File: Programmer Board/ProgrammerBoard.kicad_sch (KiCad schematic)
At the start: 9 parts

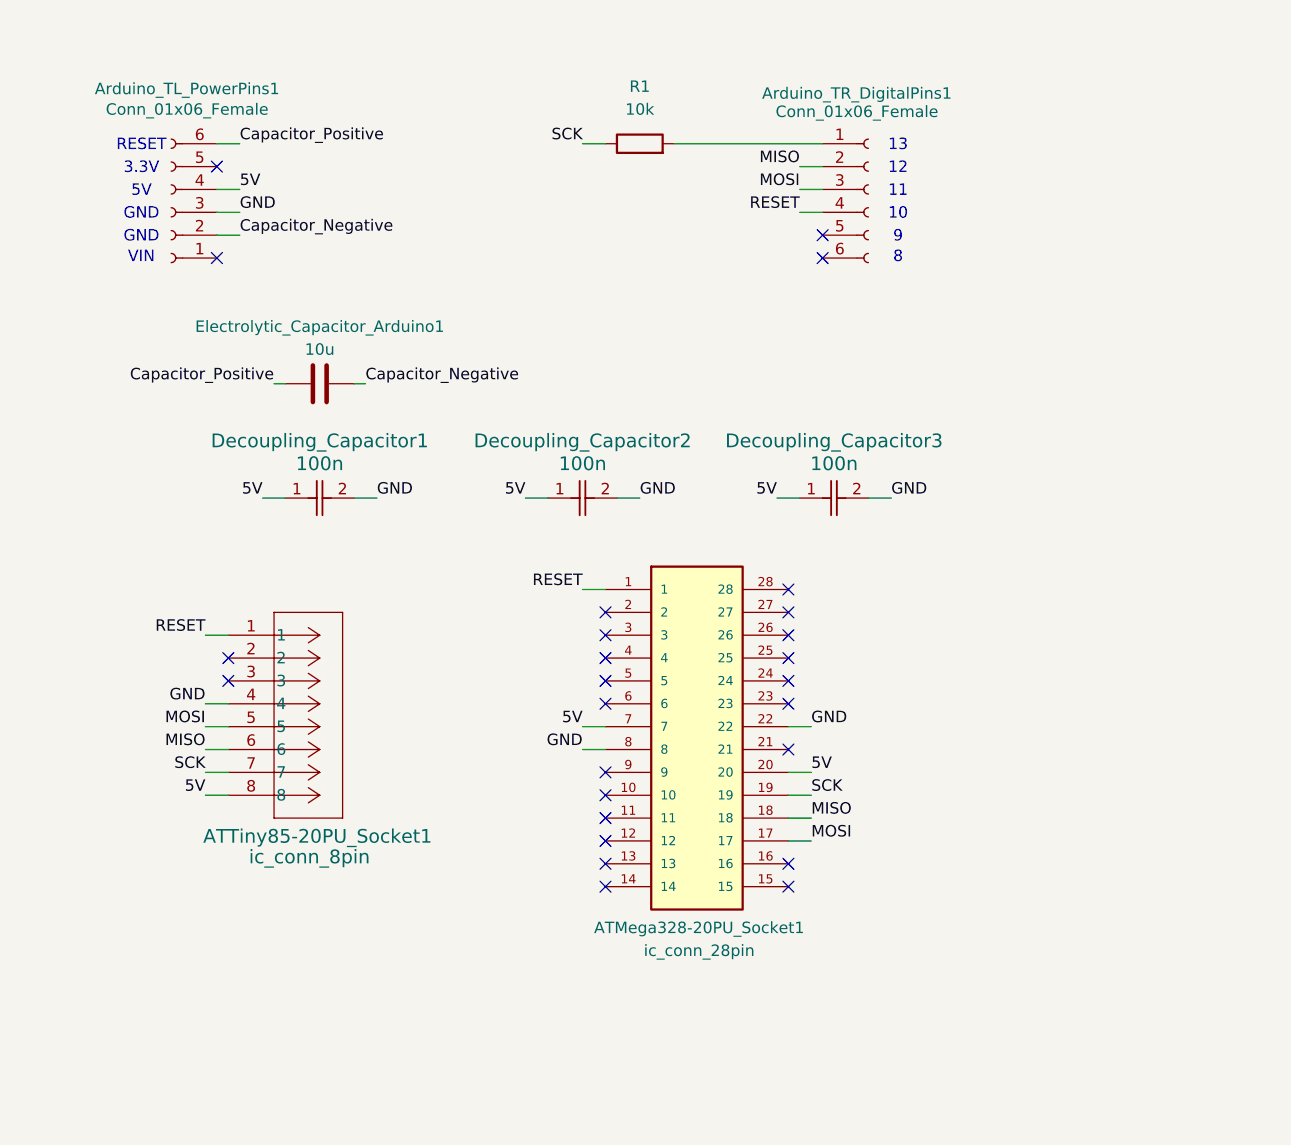
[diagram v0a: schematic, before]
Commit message: Added Header Socket Pins 1x4, 1x6, 1x8
- For flush attachment to Arduino Uno R3
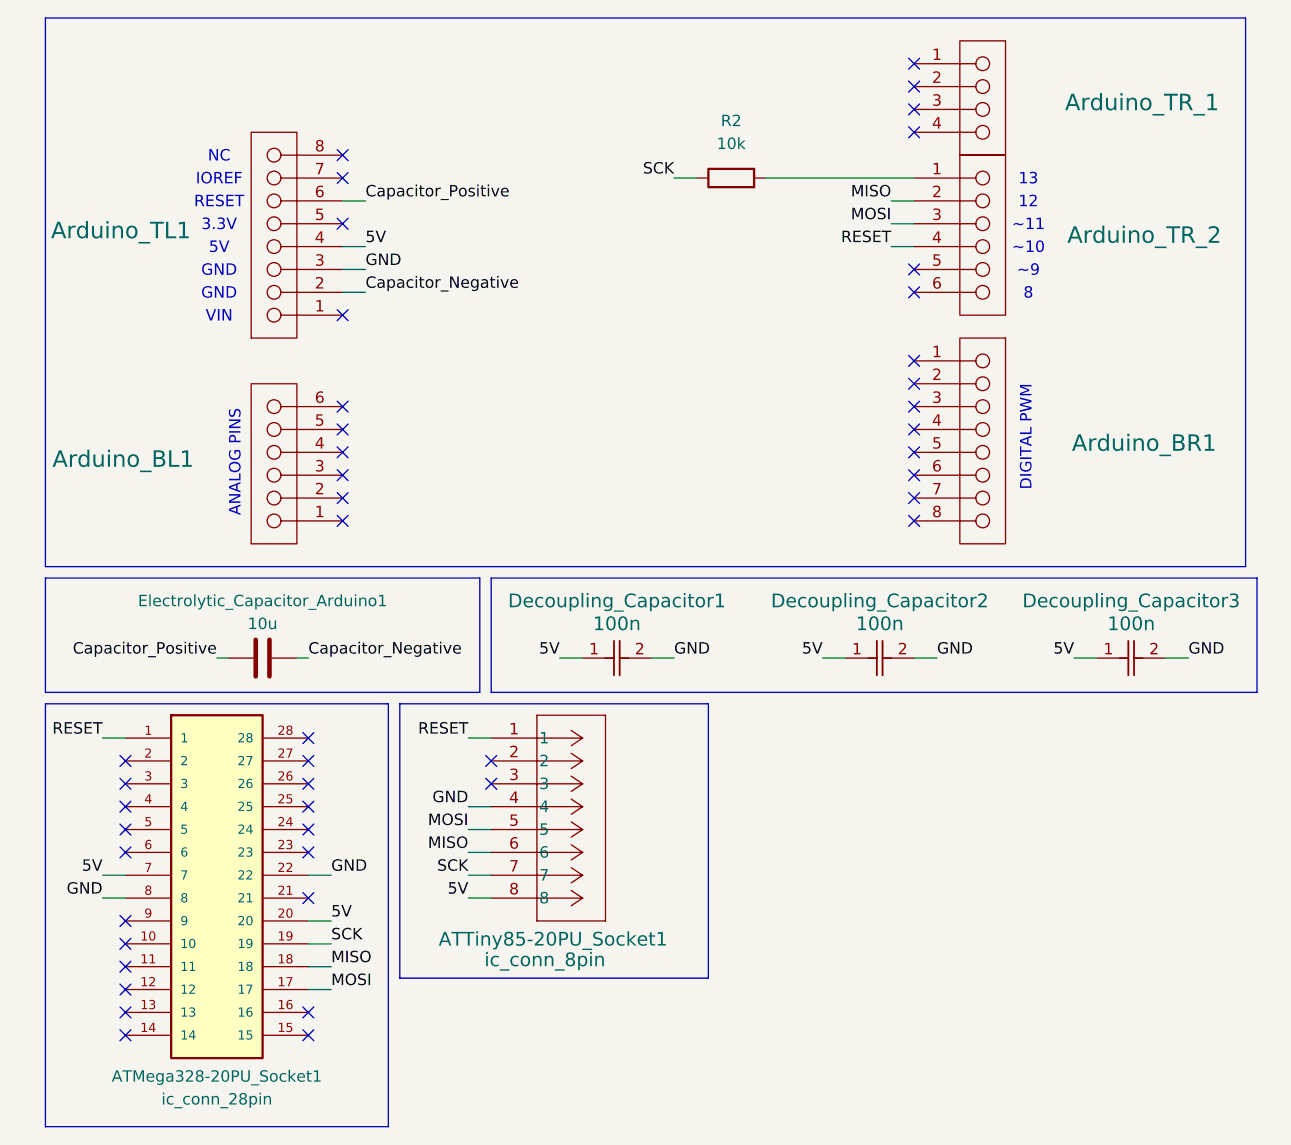
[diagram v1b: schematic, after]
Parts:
- removed Arduino_TL_PowerPins1, Arduino_TR_DigitalPins1: Conn_01x06_Female, rsx_headers:PinSocket_1x06_P2.54mm_Vertical, symbol rsx_header:Conn_01x06_Female
- removed R1: 10k, rsx_resistors:R_0603_1608Metric, symbol rsx_Resistors:10k
- added Arduino_BL1, Arduino_TR_2: header_1x6_arduino, Connector_PinHeader_2.54mm:PinHeader_1x06_P2.54mm_Vertical, symbol rsx_header:header_1x6_arduino
- added Arduino_BR1, Arduino_TL1: header_1x8_arduino, Connector_PinHeader_2.54mm:PinHeader_1x08_P2.54mm_Vertical, symbol rsx_header:header_1x8_arduino
- added Arduino_TR_1: header_1x4_arduino, Connector_PinHeader_2.54mm:PinHeader_1x04_P2.54mm_Vertical, symbol rsx_header:header_1x4_arduino
- added R2: 10k, rsx_resistors:R_0603_1608Metric, symbol rsx_Resistors:10k
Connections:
- net 5V: now also Arduino_TL1.4
- net Capacitor_Negative: now also Arduino_TL1.2
- net Capacitor_Positive: now also Arduino_TL1.6
- net GND: now also Arduino_TL1.3
- net MISO: now also Arduino_TR_2.2
- net MOSI: now also Arduino_TR_2.3
- net RESET: now also Arduino_TR_2.4
- net SCK: now also R2.1
- new net: Arduino_TR_2.1, R2.2
- no-connect marks 26 -> 46
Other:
- note added: "ANALOG PINS"
- note added: "DIGITAL PWM"
- note added: "IOREF"
- note added: "NC"
- note added: "~10"
- note added: "~11"
- note added: "~9"
- note removed: "10"
- note removed: "11"
- note removed: "9"
- moved on the sheet: ATMega328-20PU_Socket1, ATTiny85-20PU_Socket1, Decoupling_Capacitor1, Decoupling_Capacitor2, Decoupling_Capacitor3, Electrolytic_Capacitor_Arduino1
